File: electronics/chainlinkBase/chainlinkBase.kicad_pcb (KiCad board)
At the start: 2 copper layers, 98.4 x 190.5 mm, 128 parts, among them J101 Power In, J102 RELAY, J103 Power In, J104 RS485, J105 RS485, J106 Logic Power Out, J107 UART, J108 Output, J109 Output, J110 Output, J111 Conn_01x06_Male, J112 Conn_01x06_Male, J201 CHANNEL, J301 CHANNEL, J401 CHANNEL, J501 CHANNEL, J601 CHANNEL, SW101 SW_DIP_x04, U101 AP7361C-33E, U102 TPL7407L, U103 Buck, U104 TTGO_TDisplay, U105 MCP23017_SS, U106 SN74LV1T34DBV, U107 SP485, U108 SN74LV1T34DBV, U201 INA219BxD, U202 VN7007ALH, U301 INA219BxD, U302 VN7007ALH, U401 INA219BxD, U402 VN7007ALH, U501 INA219BxD, U502 VN7007ALH, U601 INA219BxD, U602 VN7007ALH

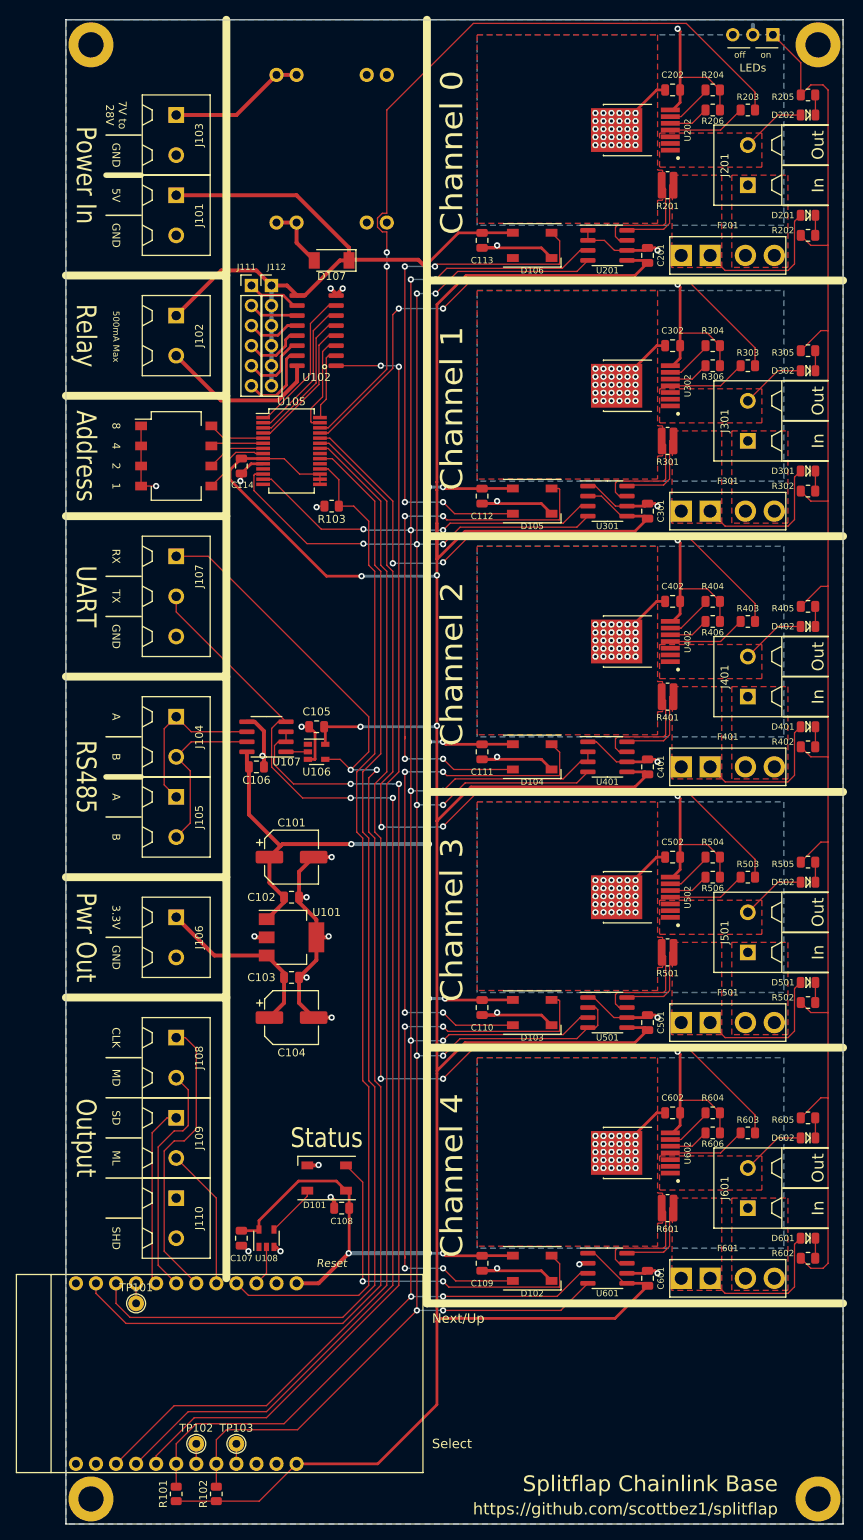
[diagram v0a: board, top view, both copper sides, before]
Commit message: Add pull-down for load switches, move LED jumpers and make solder-bridgeable
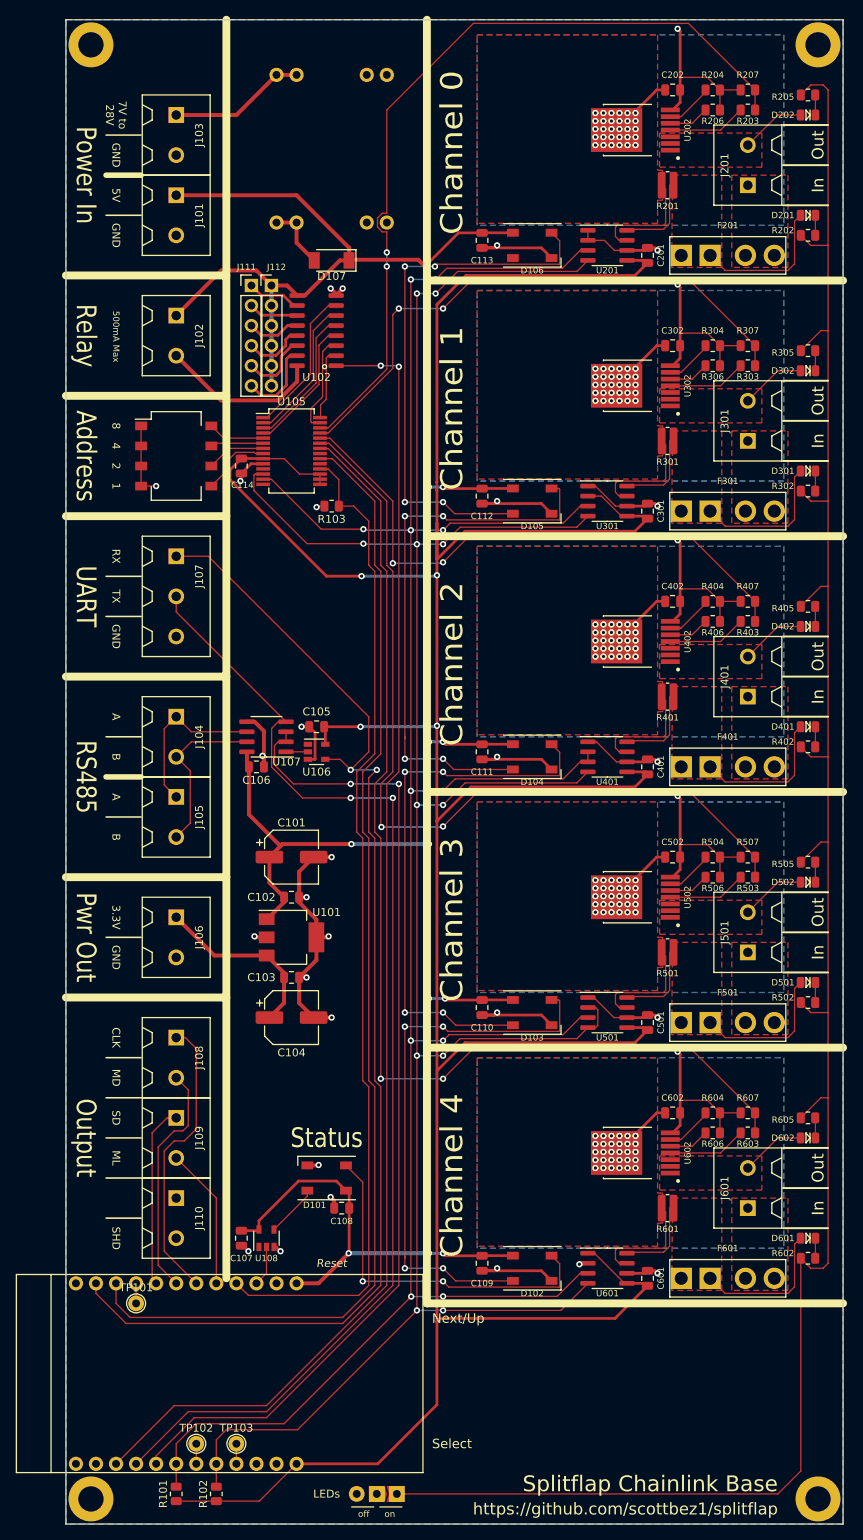
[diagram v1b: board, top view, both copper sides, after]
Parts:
- added R207: 15k, Resistor_SMD:R_0805_2012Metric, F.Cu at (111.8, 34.3)
- added R307: 15k, Resistor_SMD:R_0805_2012Metric, F.Cu at (111.8, 66.7)
- added R407: 15k, Resistor_SMD:R_0805_2012Metric, F.Cu at (111.8, 99.1)
- added R507: 15k, Resistor_SMD:R_0805_2012Metric, F.Cu at (111.8, 131.4)
- added R607: 15k, Resistor_SMD:R_0805_2012Metric, F.Cu at (111.8, 163.8)
- JP101: footprint Connector_PinHeader_2.54mm:PinHeader_1x03_P2.54mm_Vertical -> ModifiedSymbols:PinHeader_1x03_P2.54mm_Vertical_SolderJumper
- moved JP101 190.8 mm to (67.3, 212.1)
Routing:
- net /LED_GND: track 200.1 -> 270.3 mm
- net GND: track 272.2 -> 284.0 mm

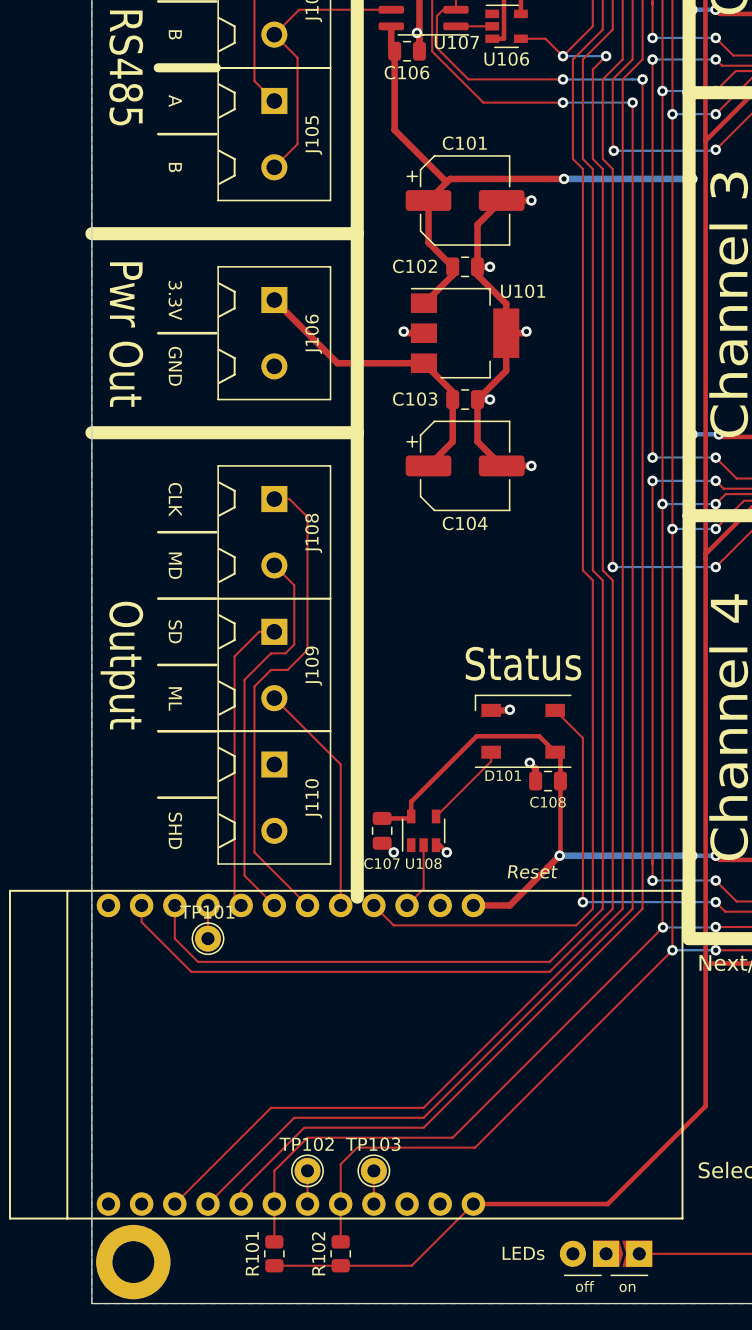
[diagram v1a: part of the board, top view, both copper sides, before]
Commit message: Update Chainlink Base electronics to fix pinout mixup (#183)
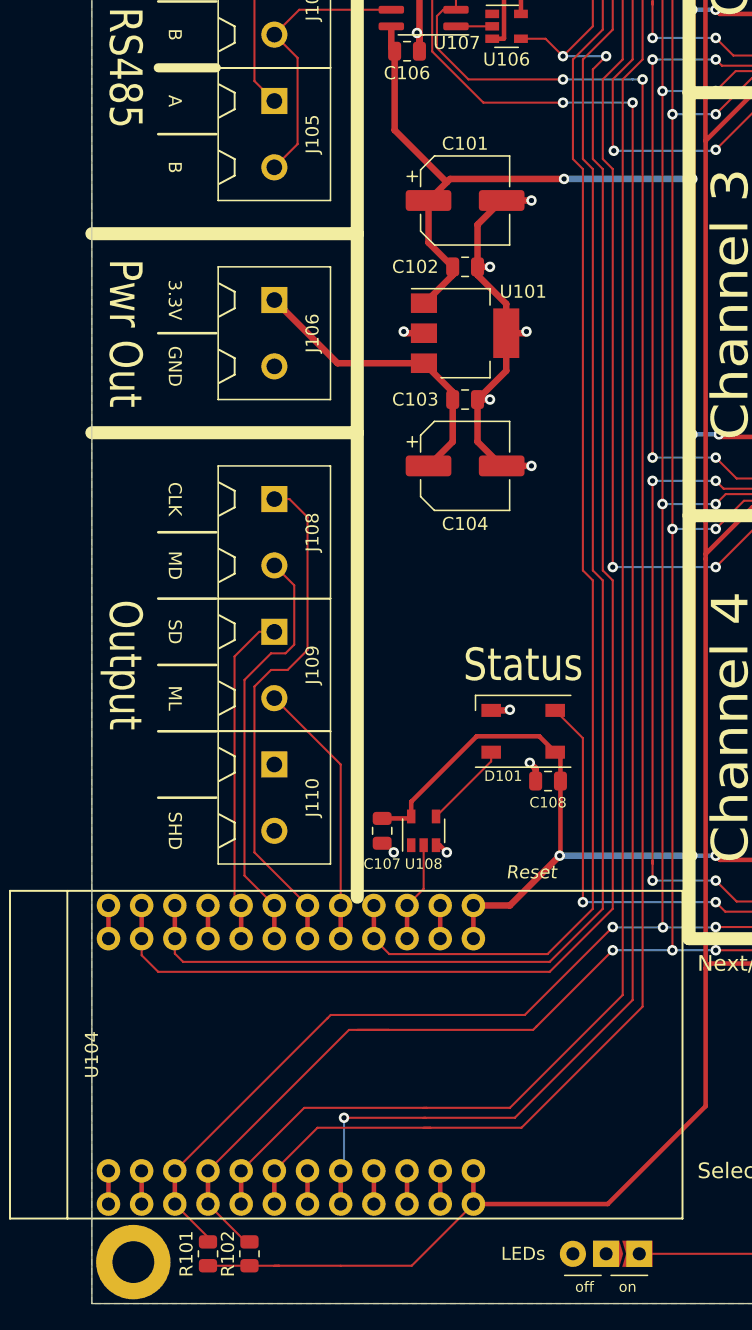
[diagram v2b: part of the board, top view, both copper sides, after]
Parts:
- removed TP101, TP102, TP103: TestPoint_Small, TestPoint:TestPoint_THTPad_D2.0mm_Drill1.0mm
- U104: footprint ESP32:T-DISPLAY -> ESP32:T-DISPLAY_extra_pins
- moved R102 6.98 mm to (37.5, 212.1)
- moved R101 5.08 mm to (34.3, 212.1)
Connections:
- U104 pad 24: (no net) -> Net-(U104-Pad24)
- U104 pad 3: /MASTER_EN -> /SDA
- U104 pad 4: /TX -> /SCL
- U104 pad 5: /RS485_DRIVE_EN -> /MASTER_EN
- U104 pad 6: /SDA -> /RS485_DRIVE_EN
- U104 pad 8: /SCL -> /TX
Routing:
- net /SCL: track 314.4 -> 328.1 mm, vias 11 -> 12
- net GND: track 284.0 -> 296.7 mm
- net /SDA: track 313.6 -> 322.3 mm, vias 11 -> 12
- net +3V3: track 415.6 -> 423.6 mm
- net /RX: track 154.8 -> 158.8 mm
- net /MCP_RESET: track 127.5 -> 130.8 mm
- net /RS485_DRIVE_EN: track 126.3 -> 129.6 mm
- net /MOTOR_DATA: track 29.8 -> 32.4 mm
- net Net-(U104-Pad24): track 0.00 -> 2.54 mm
- net /SENSOR_DATA: track 23.1 -> 25.6 mm
- net /RGB_LEDS_3V3: track 5.14 -> 7.68 mm
- net /LATCH: track 18.0 -> 20.5 mm
- net /CLOCK: track 37.0 -> 39.5 mm
- net +5V: track 345.1 -> 347.6 mm
- net /TX: track 149.3 -> 147.0 mm, vias 2 -> 3
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
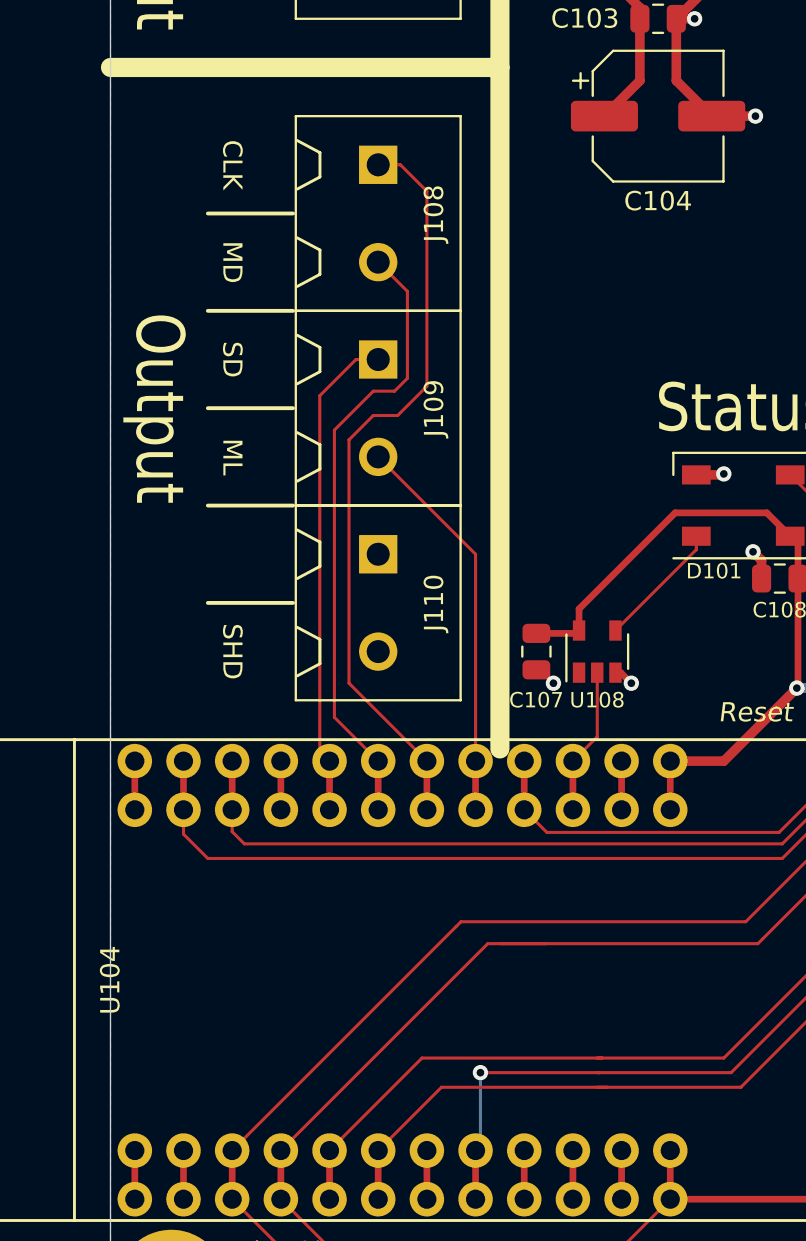
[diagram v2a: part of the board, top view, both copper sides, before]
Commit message: Change Chainlink data connections from screw terminals to IDC (#189)
- Replace screw terminals with 2x4 IDC connectors (alternating ground) on Driver, Base, and Tester. Fixes #179
- Change Chainlink Driver Tester to all 1mm pogo pins
- Create new "Buddy" boards for connecting IDC/ribbon cable to T-Display or a breadboard
- Big readme cleanup and reorganization for clarity (hopefully!)
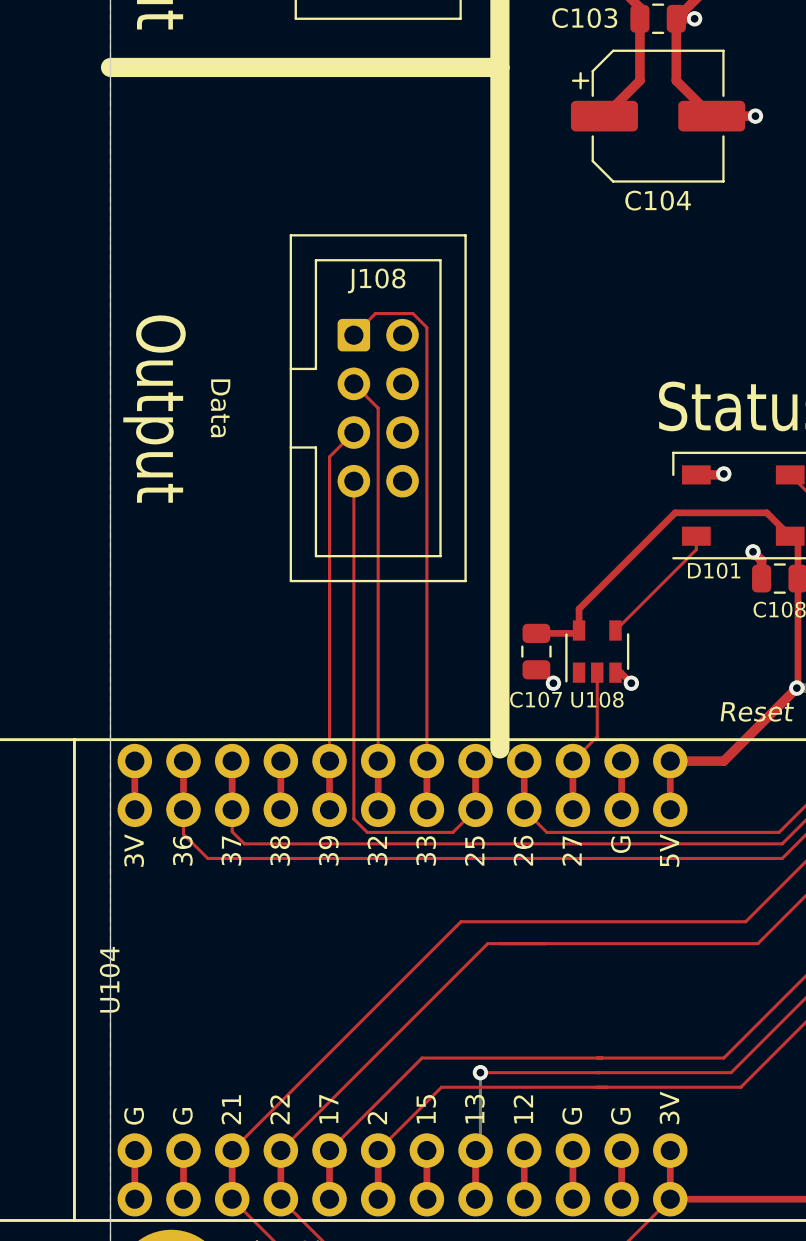
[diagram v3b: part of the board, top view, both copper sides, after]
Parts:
- removed J109, J110: Output, ScrewTerminals:Generic-5.08-2P
- J108: value Output -> Conn_02x04_Odd_Even; footprint ScrewTerminals:Generic-5.08-2P -> ModifiedSymbols:IDC-Header_2x04_P2.54mm_Vertical
- U104: footprint ESP32:T-DISPLAY_extra_pins -> ESP32:T-DISPLAY_extra_pins_labeled
- moved J108 8.98 mm to (38.1, 163.2), turned to 0 degrees
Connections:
- J108 pad 2: /MOTOR_DATA -> GND
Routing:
- net /CLOCK: track 39.5 -> 29.7 mm
- net /MOTOR_DATA: track 32.4 -> 22.8 mm
- net /LATCH: track 20.5 -> 27.3 mm
- net /SENSOR_DATA: track 25.6 -> 20.2 mm
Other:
- board text added: "Data"
- board text removed: "CLK"
- board text removed: "MD"
- board text removed: "ML"
- board text removed: "SD"
- board text removed: "SHD"

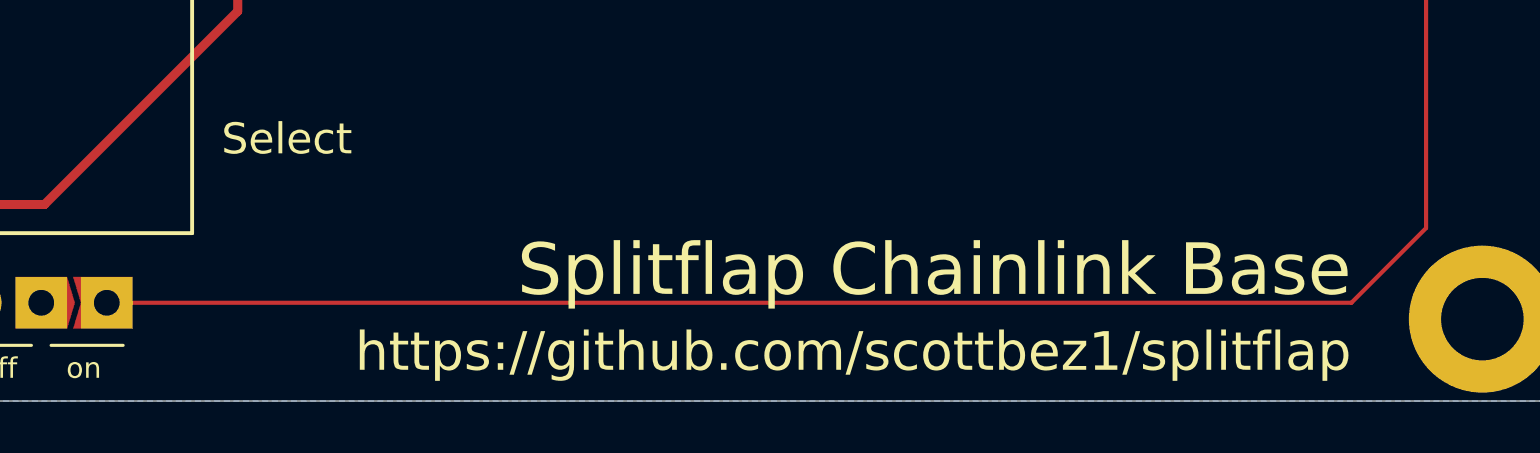
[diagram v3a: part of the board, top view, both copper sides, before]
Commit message: Add version numbers to chainlink PCBs
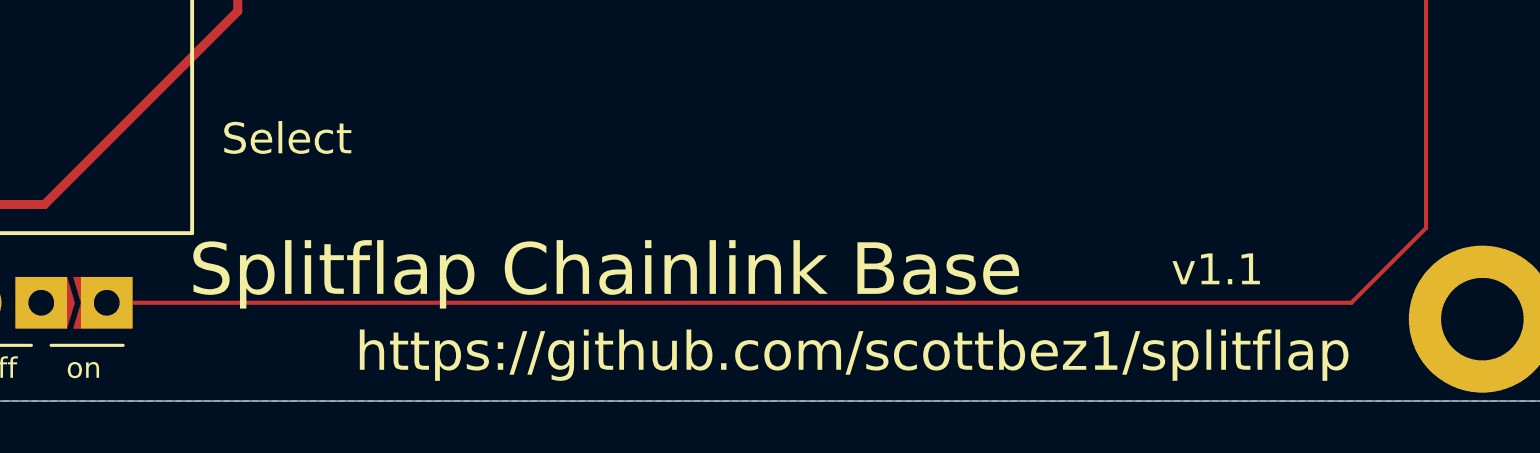
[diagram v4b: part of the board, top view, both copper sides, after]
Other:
- board text added: "v1.1"
